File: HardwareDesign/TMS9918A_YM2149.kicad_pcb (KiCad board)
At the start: 2 copper layers, 150 x 90 mm, 46 parts, among them J001 Conn_02x40_Odd_Even, J701 RCJ-044, J702 Conn_01x02, J801 Conn_01x02, J802 Conn_02x09_Odd_Even, J803 SJ1-3525N, Q701 2N4401, U701 TMS9918A, U702 74HCT04, U703 74HCT32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

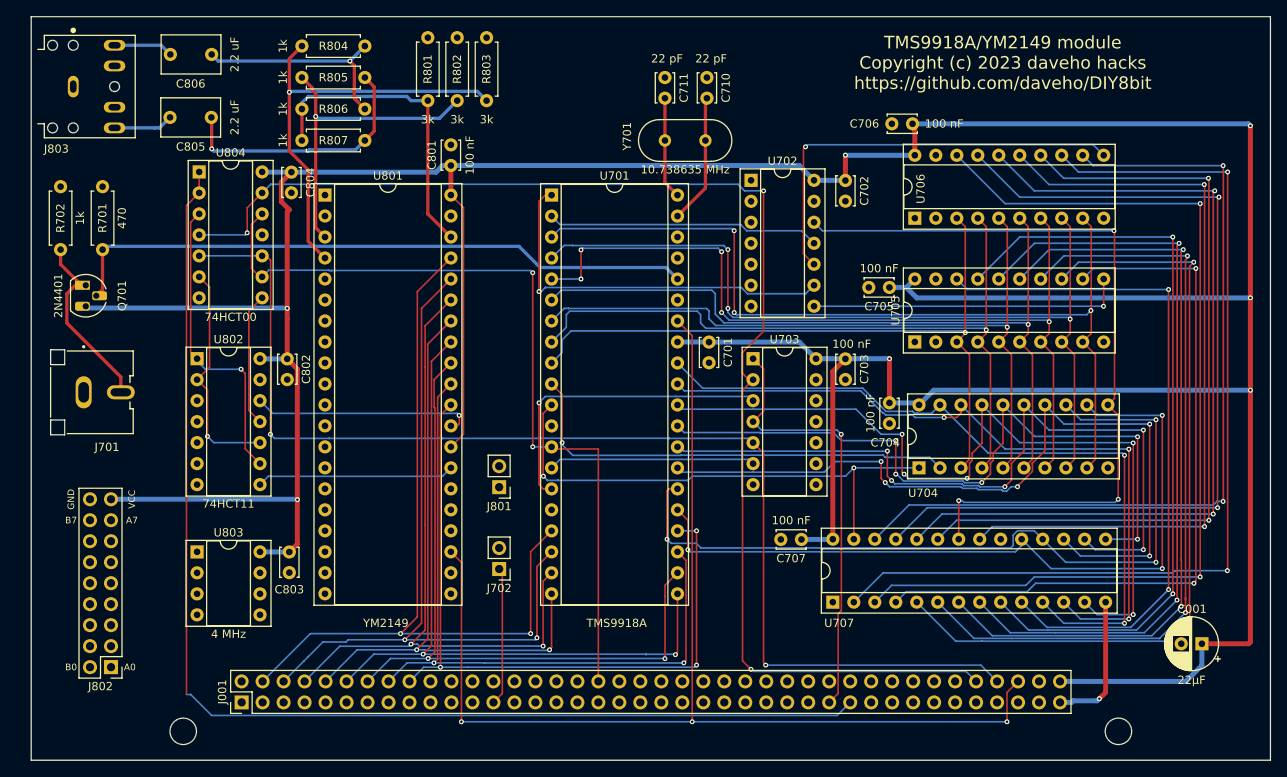
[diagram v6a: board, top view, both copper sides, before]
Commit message: all signals routed, DRC is clean
Almost ready to fab?
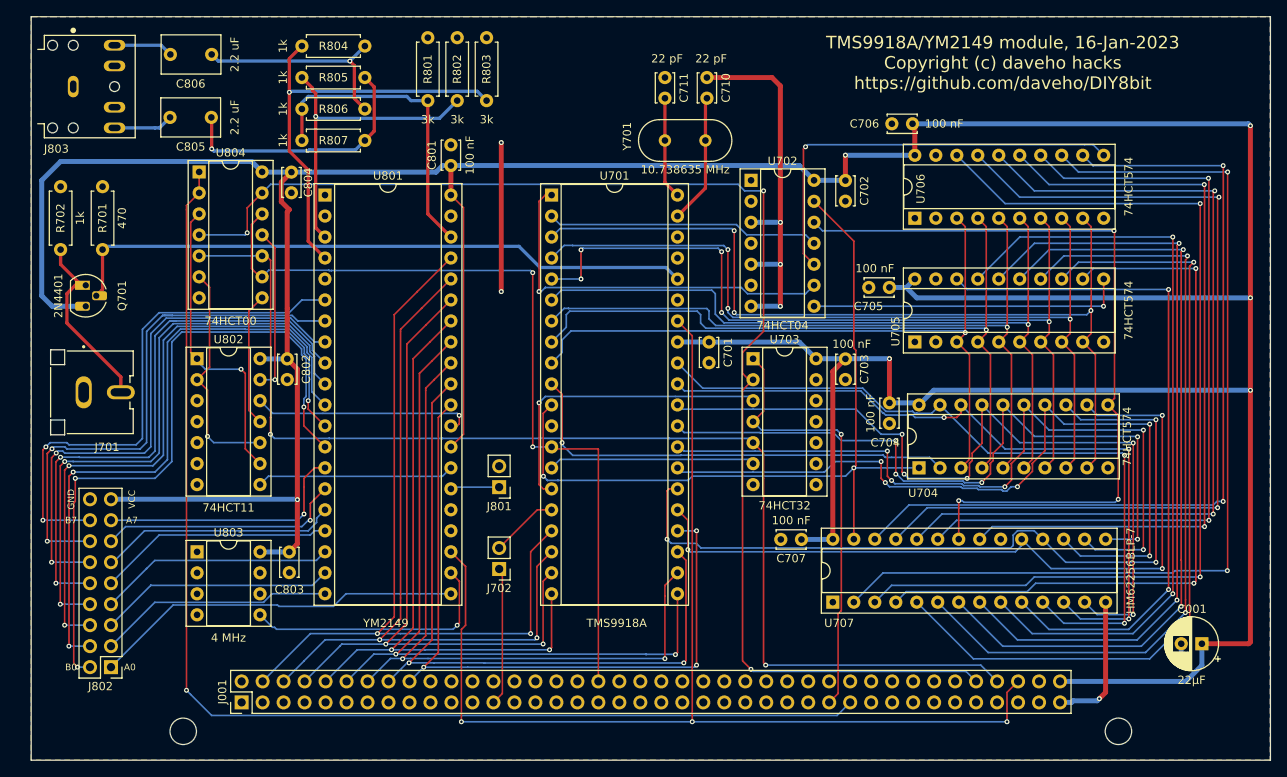
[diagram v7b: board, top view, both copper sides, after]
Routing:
- net /YM2149_Sound/IOB0: track 0.00 -> 81.9 mm, vias 0 -> 3
- net /YM2149_Sound/IOB1: track 0.00 -> 78.8 mm, vias 0 -> 3
- net /YM2149_Sound/IOB2: track 0.00 -> 75.5 mm, vias 0 -> 2
- net /YM2149_Sound/IOB3: track 0.00 -> 72.4 mm, vias 0 -> 2
- net /YM2149_Sound/IOB4: track 0.00 -> 70.0 mm, vias 0 -> 2
- net GND: track 16.9 -> 83.9 mm, vias 1 -> 7
- net /YM2149_Sound/IOB5: track 0.00 -> 66.8 mm, vias 0 -> 2
- net /YM2149_Sound/IOB6: track 0.00 -> 65.9 mm, vias 0 -> 2
- net /YM2149_Sound/IOB7: track 0.00 -> 63.8 mm, vias 0 -> 2
- net /YM2149_Sound/IOA0: track 0.00 -> 45.0 mm
- net /TMS9918ADisplay/VR/~{W}: track 64.0 -> 98.5 mm
- net Net-(U801-Pad22): track 0.00 -> 31.7 mm, vias 0 -> 1
- net /YM2149_Sound/IOA7: track 0.00 -> 31.1 mm, vias 0 -> 1
- net /YM2149_Sound/IOA6: track 0.00 -> 29.7 mm, vias 0 -> 1
- net /YM2149_Sound/IOA5: track 0.00 -> 28.8 mm
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- added copper zone on B.Cu, net GND
- added copper zone on F.Cu, net GND
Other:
- board text added: "TMS9918A/YM2149 module, 16-Jan-2023 Copyright (c) daveho hacks https://github.com/daveho/DIY8bit"
- board text removed: "TMS9918A/YM2149 module Copyright (c) 2023 daveho hacks https://github.com/daveho/DIY8bit"

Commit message: various tweaks to front silkscreen
I think this is probably ready to fab.
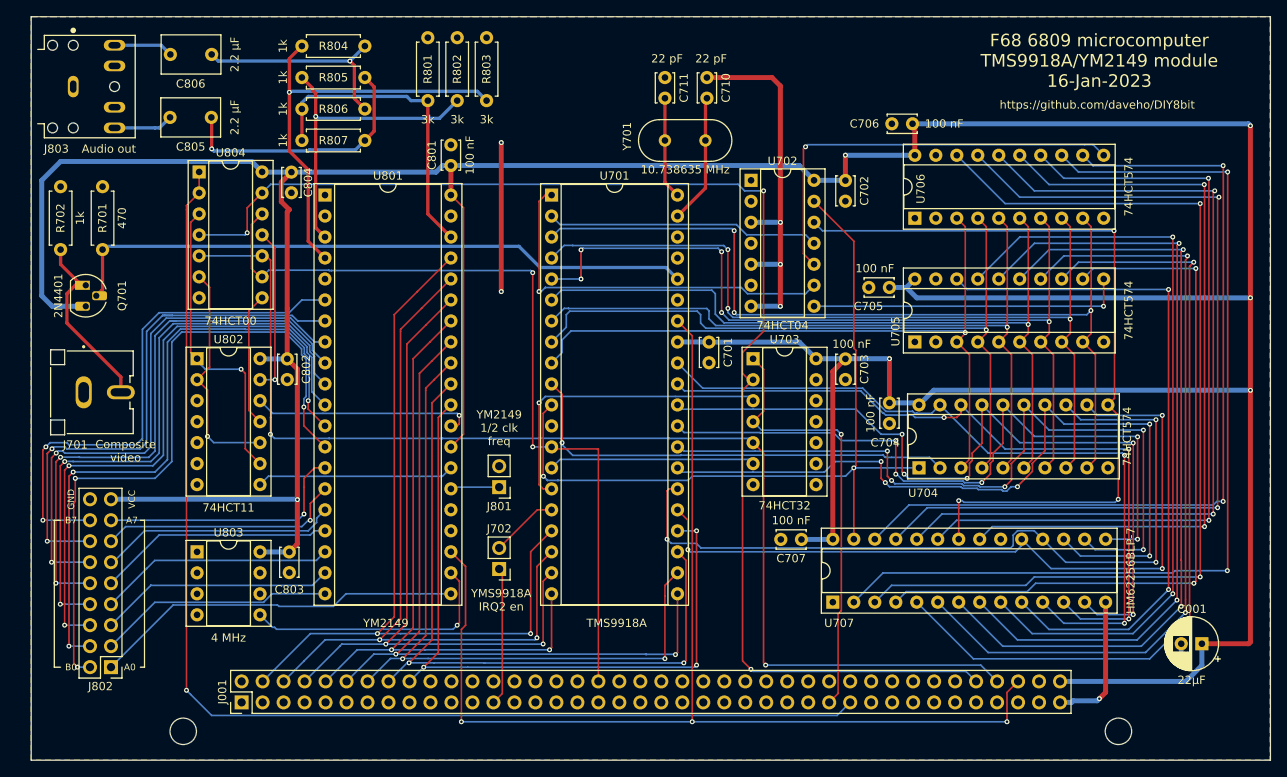
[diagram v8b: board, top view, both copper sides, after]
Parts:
- C805, C806: value 2.2 uF -> 2.2 μF
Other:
- board text added: "Audio out"
- board text added: "Composite video"
- board text added: "F68 6809 microcomputer TMS9918A/YM2149 module 16-Jan-2023"
- board text added: "YM2149 1/2 clk freq"
- board text added: "YMS9918A IRQ2 en"
- board text added: "https://github.com/daveho/DIY8bit"
- board text removed: "TMS9918A/YM2149 module, 16-Jan-2023 Copyright (c) daveho hacks https://github.com/daveho/DIY8bit"
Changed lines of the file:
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@@
       (effects (font (size 1 1) (thickness 0.15)))
     )
-    (fp_text value "2.2 uF" (at -2.794 0 90) (layer "F.SilkS")
+    (fp_text value "2.2 μF" (at -2.794 0 90) (layer "F.SilkS")
       (effects (font (size 1 1) (thickness 0.15)))
     )
@@
     (property "Sheetname" "TMS9918ADisplay")
     (attr through_hole)
-    (fp_text reference "J701" (at -2.825 -6.635) (layer "F.SilkS")
+    (fp_text reference "J701" (at 1.016 -6.35) (layer "F.SilkS")
       (effects (font (size 1 1) (thickness 0.15)))
     )
@@
     (property "Sheetname" "TMS9918ADisplay")
     (attr through_hole)
-    (fp_text reference "J702" (at 0 -2.33) (layer "F.SilkS")
+    (fp_text reference "J702" (at 0 4.876) (layer "F.SilkS")
       (effects (font (size 1 1) (thickness 0.15)))
     )
@@
       (effects (font (size 1 1) (thickness 0.15)))
     )
-    (fp_text value "2.2 uF" (at -2.834 0 90) (layer "F.SilkS")
+    (fp_text value "2.2 μF" (at -2.834 0 90) (layer "F.SilkS")
       (effects (font (size 1 1) (thickness 0.15)))
     )
@@
       (effects (font (size 1 1) (thickness 0.15)))
     )
-    (fp_text value "Conn_01x02" (at 0 4.87) (layer "F.Fab")
+    (fp_text value "Conn_01x02" (at 0 4.87 90) (layer "F.Fab")
       (effects (font (size 1 1) (thickness 0.15)))
     )
@@
     )
   )
+  (gr_line (start 66.294 137.16) (end 67.056 137.16) (layer "F.SilkS") (width 0.1524))
+  (gr_line (start 77.216 119.38) (end 77.216 137.16) (layer "F.SilkS") (width 0.1524))
+  (gr_line (start 77.216 137.16) (end 76.708 137.16) (layer "F.SilkS") (width 0.1524))
+  (gr_line (start 67.056 119.38) (end 66.294 119.38) (layer "F.SilkS") (width 0.1524))
+  (gr_line (start 66.294 119.38) (end 66.294 137.16) (layer "F.SilkS") (width 0.1524))
+  (gr_line (start 76.708 119.38) (end 77.216 119.38) (layer "F.SilkS") (width 0.1524))
   (gr_line (start 213.5 58.42) (end 63.5 58.42) (layer "Edge.Cuts") (width 0.0381))
   (gr_line (start 213.5 148.42) (end 213.5 58.42) (layer "Edge.Cuts") (width 0.0381))
   (gr_line (start 63.5 148.42) (end 213.5 148.42) (layer "Edge.Cuts") (width 0.0381))
   (gr_line (start 63.5 58.42) (end 63.5 148.42) (layer "Edge.Cuts") (width 0.0381))
+  (gr_text "https://github.com/daveho/DIY8bit" (at 192.532 69.088) (layer "F.SilkS")
+    (effects (font (size 1 1) (thickness 0.25)))
+  )
   (gr_text "A0" (at 75.438 137.16) (layer "F.SilkS")
     (effects (font (size 0.8 0.8) (thickness 0.2)))
   )
-  (gr_text "TMS9918A/YM2149 module, 16-Jan-2023\nCopyright (c) daveho hacks\nhttps://github.com/daveho/DIY8bit" (at 181.102 64.008) (layer "F.SilkS")
+  (gr_text "Composite\nvideo" (at 74.93 110.998) (layer "F.SilkS")
+    (effects (font (size 1 1) (thickness 0.25)))
+  )
+  (gr_text "F68 6809 microcomputer\nTMS9918A/YM2149 module\n16-Jan-2023" (at 192.786 63.754) (layer "F.SilkS")
     (effects (font (size 1.524 1.524) (thickness 0.3048)))
+  )
+  (gr_text "Audio out" (at 72.898 74.422) (layer "F.SilkS")
+    (effects (font (size 1 1) (thickness 0.25)))
   )
   (gr_text "VCC" (at 75.692 116.84 90) (layer "F.SilkS")
     (effects (font (size 0.8 0.8) (thickness 0.2)))
   )
+  (gr_text "YMS9918A\nIRQ2 en" (at 120.396 129.032) (layer "F.SilkS")
+    (effects (font (size 1 1) (thickness 0.25)))
+  )
   (gr_text "B0" (at 68.326 137.16) (layer "F.SilkS")
     (effects (font (size 0.8 0.8) (thickness 0.2)))
@@
     (effects (font (size 0.8 0.8) (thickness 0.2)))
   )
+  (gr_text "YM2149\n1/2 clk\nfreq" (at 120.142 108.204) (layer "F.SilkS")
+    (effects (font (size 1 1) (thickness 0.25)))
+  )
   (gr_text "GND" (at 68.326 116.84 90) (layer "F.SilkS")
